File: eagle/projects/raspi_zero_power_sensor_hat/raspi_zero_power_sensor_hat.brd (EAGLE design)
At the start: 65 x 30 mm, 156 parts, among them J301 MOL-SL-2-RA, J302 USB_MICROB_RECPT, J401 MOL-SL-2-RA, J402 MOL-SL-2-V, J601 RECEPTACLE-2x5-2.54MM, J602 MOL-SL-4-RA, J603 MOL-SL-3-V, J604 RECEPTACLE-2x3-2.54MM, Q301 SSM6N7002KFU, Q401 SSM6N7002KFU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

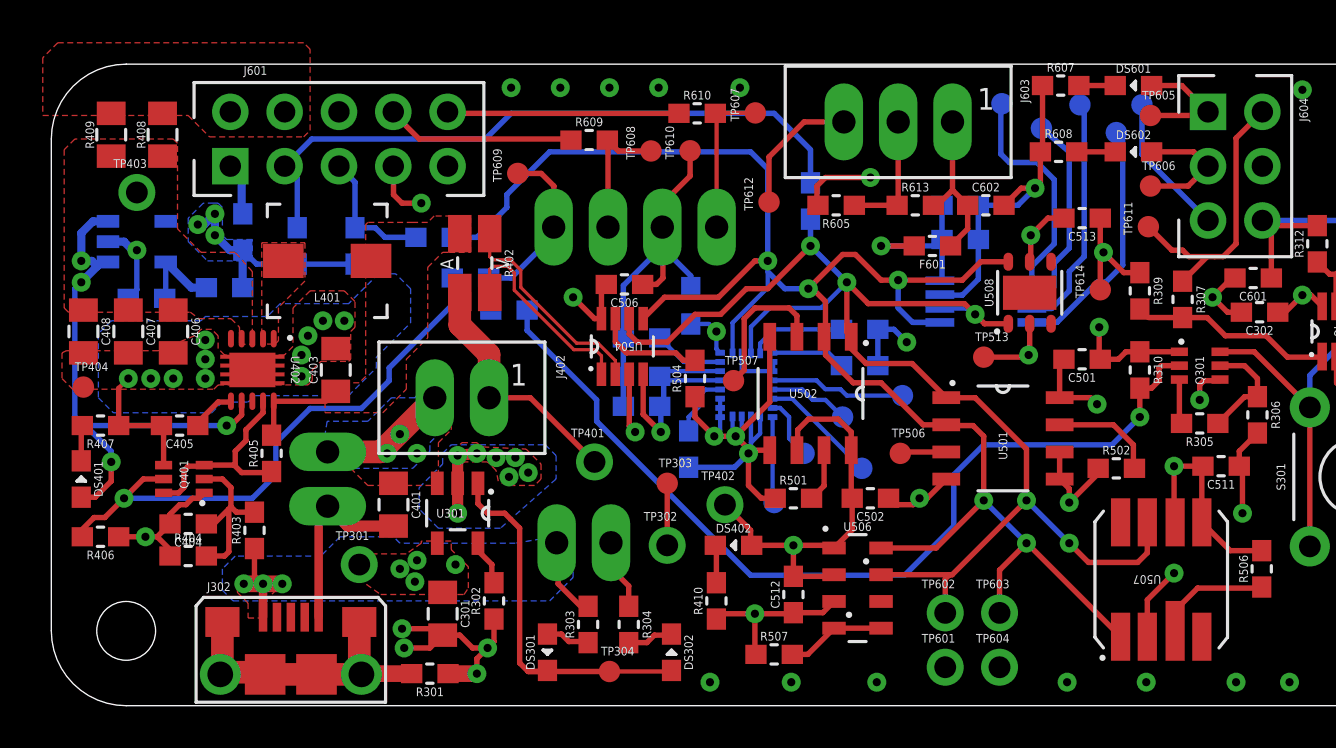
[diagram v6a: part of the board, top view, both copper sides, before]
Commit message: changed board outline to be added only on the board. modified the Raspi outline schematic symbol to only include the mouting holes
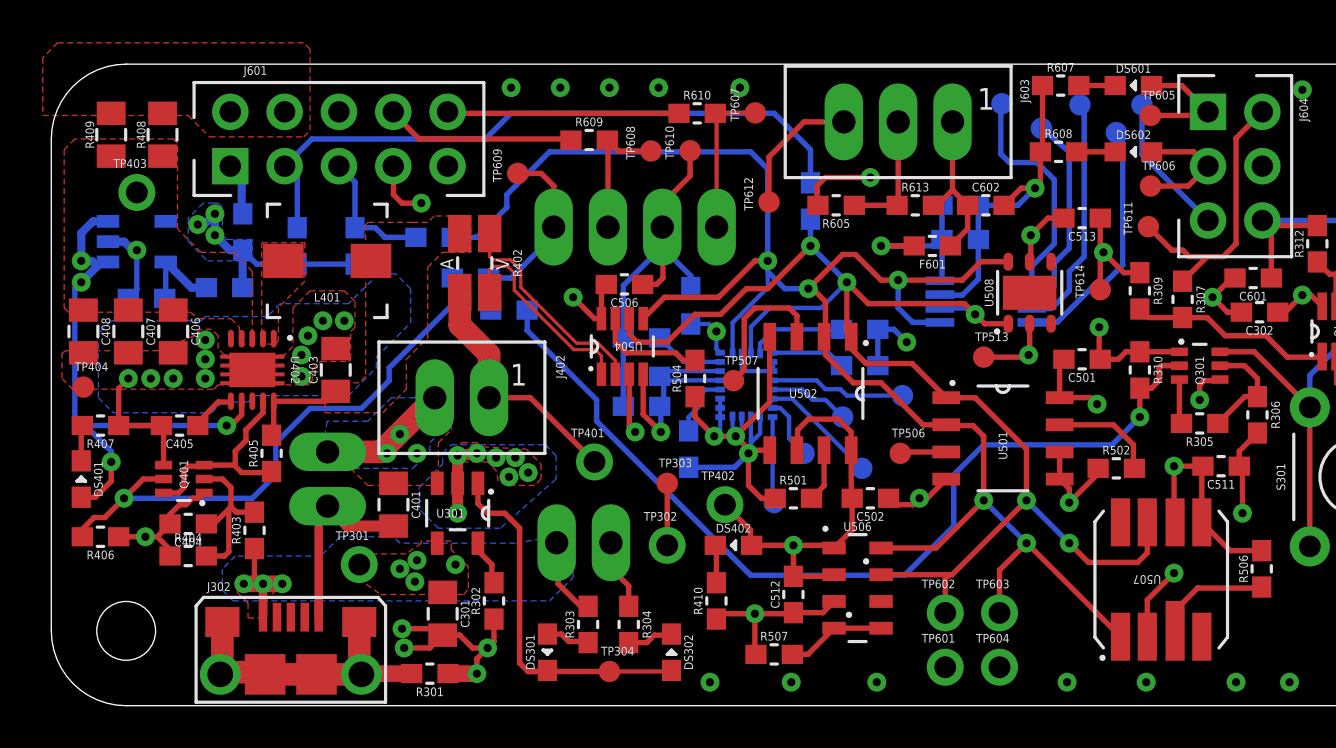
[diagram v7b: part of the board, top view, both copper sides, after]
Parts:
- removed OUTLINE601: RASPI-ZERO-3STANDOFFS-0CAM, daqcs:RASPI_ZERO_3STANDOFFS
- added OUTLINE1: RASPI_ZERO_OUTLINE_3S0C_ONLY, daqcs:RASPI_ZERO_3STANDOFFS_ONLY
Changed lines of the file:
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@@
 <grid distance="0.1" unitdist="mm" unit="mm" style="lines" multiple="1" display="no" altdistance="0.01" altunitdist="mm" altunit="mm"/>
 <layers>
-<layer number="1" name="Top" color="4" fill="1" visible="no" active="yes"/>
+<layer number="1" name="Top" color="4" fill="1" visible="yes" active="yes"/>
 <layer number="2" name="GND" color="26" fill="1" visible="no" active="yes"/>
 <layer number="3" name="Route3" color="4" fill="3" visible="no" active="no"/>
@@
 <layer number="19" name="Unrouted" color="6" fill="1" visible="no" active="yes"/>
 <layer number="20" name="Dimension" color="15" fill="1" visible="yes" active="yes"/>
-<layer number="21" name="tPlace" color="7" fill="1" visible="no" active="yes"/>
+<layer number="21" name="tPlace" color="7" fill="1" visible="yes" active="yes"/>
 <layer number="22" name="bPlace" color="23" fill="1" visible="no" active="yes"/>
-<layer number="23" name="tOrigins" color="15" fill="1" visible="no" active="yes"/>
+<layer number="23" name="tOrigins" color="15" fill="1" visible="yes" active="yes"/>
 <layer number="24" name="bOrigins" color="15" fill="1" visible="no" active="yes"/>
-<layer number="25" name="tNames" color="7" fill="1" visible="no" active="yes"/>
+<layer number="25" name="tNames" color="7" fill="1" visible="yes" active="yes"/>
 <layer number="26" name="bNames" color="7" fill="1" visible="no" active="yes"/>
-<layer number="27" name="tValues" color="7" fill="1" visible="no" active="yes"/>
+<layer number="27" name="tValues" color="7" fill="1" visible="yes" active="yes"/>
 <layer number="28" name="bValues" color="7" fill="1" visible="no" active="yes"/>
-<layer number="29" name="tStop" color="7" fill="3" visible="no" active="yes"/>
+<layer number="29" name="tStop" color="7" fill="3" visible="yes" active="yes"/>
 <layer number="30" name="bStop" color="7" fill="6" visible="no" active="yes"/>
-<layer number="31" name="tCream" color="7" fill="4" visible="no" active="yes"/>
+<layer number="31" name="tCream" color="7" fill="4" visible="yes" active="yes"/>
 <layer number="32" name="bCream" color="7" fill="5" visible="no" active="yes"/>
-<layer number="33" name="tFinish" color="6" fill="3" visible="no" active="yes"/>
+<layer number="33" name="tFinish" color="6" fill="3" visible="yes" active="yes"/>
 <layer number="34" name="bFinish" color="6" fill="6" visible="no" active="yes"/>
-<layer number="35" name="tGlue" color="7" fill="4" visible="no" active="yes"/>
+<layer number="35" name="tGlue" color="7" fill="4" visible="yes" active="yes"/>
 <layer number="36" name="bGlue" color="7" fill="5" visible="no" active="yes"/>
-<layer number="37" name="tTest" color="7" fill="1" visible="no" active="yes"/>
+<layer number="37" name="tTest" color="7" fill="1" visible="yes" active="yes"/>
 <layer number="38" name="bTest" color="7" fill="1" visible="no" active="yes"/>
-<layer number="39" name="tKeepout" color="4" fill="11" visible="no" active="yes"/>
+<layer number="39" name="tKeepout" color="4" fill="11" visible="yes" active="yes"/>
 <layer number="40" name="bKeepout" color="1" fill="11" visible="no" active="yes"/>
-<layer number="41" name="tRestrict" color="4" fill="10" visible="no" active="yes"/>
+<layer number="41" name="tRestrict" color="4" fill="10" visible="yes" active="yes"/>
 <layer number="42" name="bRestrict" color="1" fill="10" visible="no" active="yes"/>
 <layer number="43" name="vRestrict" color="2" fill="10" visible="no" active="yes"/>
-<layer number="44" name="Drills" color="7" fill="1" visible="no" active="yes"/>
+<layer number="44" name="Drills" color="7" fill="1" visible="yes" active="yes"/>
 <layer number="45" name="Holes" color="7" fill="1" visible="yes" active="yes"/>
-<layer number="46" name="Milling" color="3" fill="1" visible="no" active="yes"/>
-<layer number="47" name="Measures" color="7" fill="1" visible="no" active="yes"/>
-<layer number="48" name="Document" color="7" fill="1" visible="no" active="yes"/>
-<layer number="49" name="Reference" color="7" fill="1" visible="no" active="yes"/>
+<layer number="46" name="Milling" color="3" fill="1" visible="yes" active="yes"/>
+<layer number="47" name="Measures" color="7" fill="1" visible="yes" active="yes"/>
+<layer number="48" name="Document" color="7" fill="1" visible="yes" active="yes"/>
+<layer number="49" name="Reference" color="7" fill="1" visible="yes" active="yes"/>
 <layer number="50" name="dxf" color="7" fill="1" visible="no" active="no"/>
-<layer number="51" name="tDocu" color="14" fill="1" visible="no" active="yes"/>
+<layer number="51" name="tDocu" color="14" fill="1" visible="yes" active="yes"/>
 <layer number="52" name="bDocu" color="6" fill="1" visible="no" active="yes"/>
 <layer number="53" name="tGND_GNDA" color="7" fill="9" visible="no" active="no"/>
@@
 <board>
 <plain>
+<wire x1="3.5" y1="0" x2="0" y2="3.5" width="0" layer="20" curve="-90"/>
+<wire x1="65" y1="3.5" x2="61.5" y2="0" width="0" layer="20" curve="-90"/>
+<wire x1="61.5" y1="30" x2="65" y2="26.5" width="0" layer="20" curve="-90"/>
+<wire x1="0" y1="26.5" x2="3.5" y2="30" width="0" layer="20" curve="-90"/>
+<wire x1="3.5" y1="30" x2="61.5" y2="30" width="0" layer="20"/>
+<wire x1="65" y1="26.5" x2="65" y2="3.5" width="0" layer="20"/>
+<wire x1="61.5" y1="0" x2="3.5" y2="0" width="0" layer="20"/>
+<wire x1="0" y1="3.5" x2="0" y2="26.5" width="0" layer="20"/>
 </plain>
 <attributes>
@@
 <attribute name="DATASHEET" value="HW/docs/projects/raspi_zero_power_sensor_hat/datasheets/passives/c02e.pdf" x="48.2" y="22.8" size="1.778" layer="27" rot="R180" display="off"/>
 </element>
-<element name="OUTLINE601" library="daqcs" package="RASPI_ZERO_3STANDOFFS" value="RASPI-ZERO-3STANDOFFS-0CAM" x="0" y="0"/>
 <element name="DS601" library="daqcs" package="LED0603" value="YELLOW" x="50.6" y="29">
 <attribute name="FORWARD_CURRENT" value="20mA" x="50.6" y="29" size="1.778" layer="27" display="off"/>
@@
 <attribute name="TP_SIGNAL_NAME" value="" x="43.6" y="16.3" size="1.778" layer="27" display="off"/>
 </element>
+<element name="OUTLINE1" library="daqcs" package="RASPI_ZERO_3STANDOFFS_ONLY" value="RASPI_ZERO_OUTLINE_3S0C_ONLY" x="0" y="0"/>
 </elements>
 <signals>

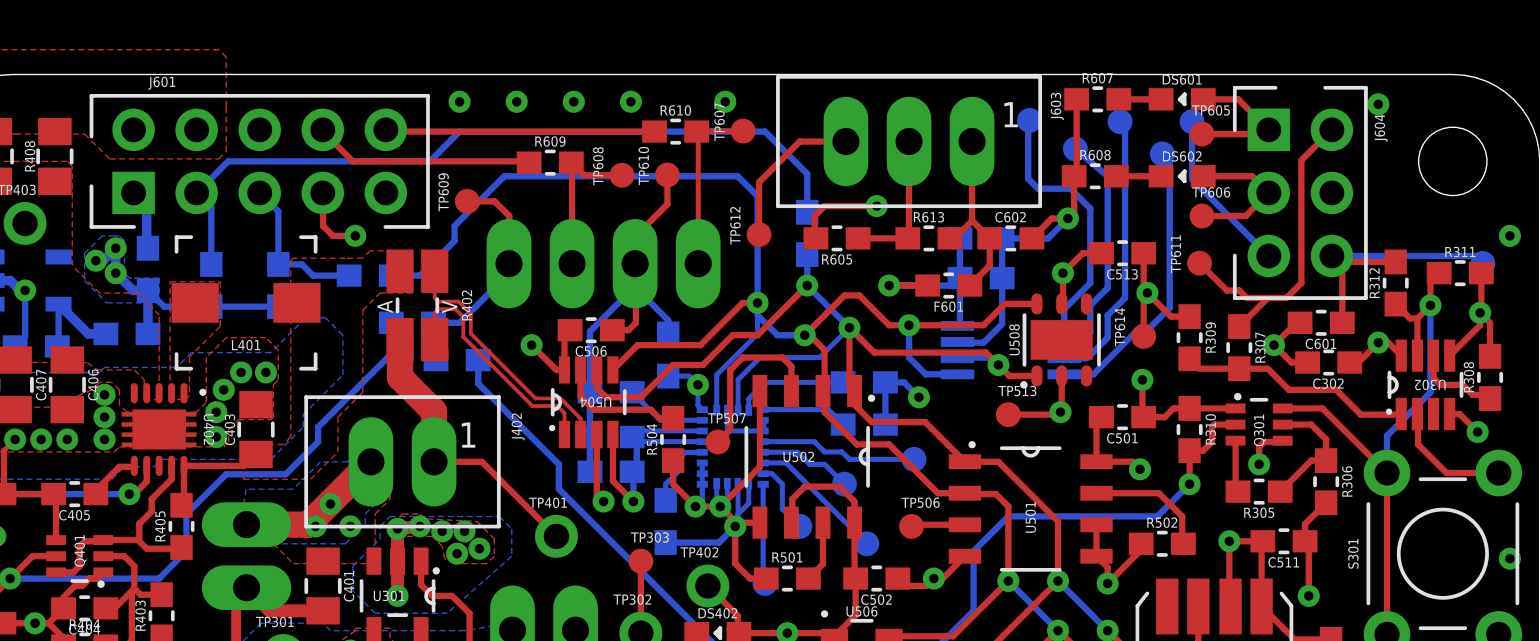
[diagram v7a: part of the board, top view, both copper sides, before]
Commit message: fixed bottom side component silk screen. SIZE * RATIO > 0.15mm
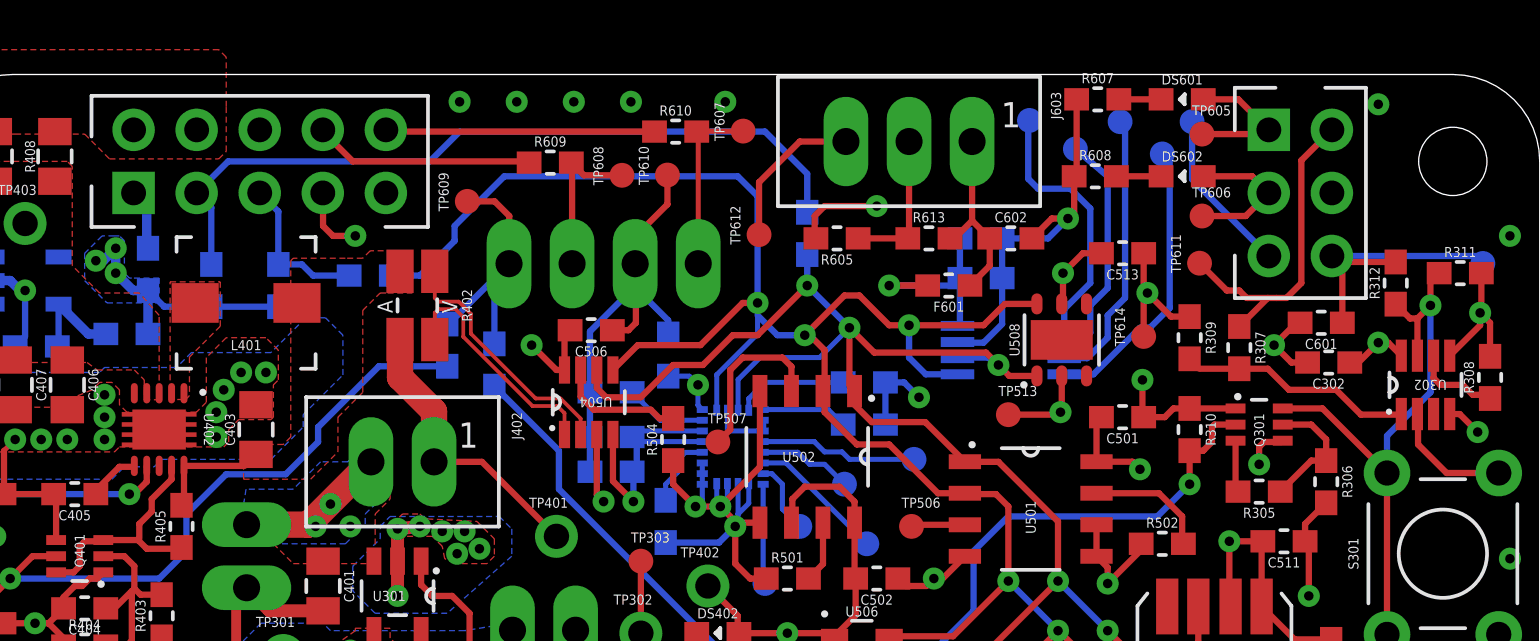
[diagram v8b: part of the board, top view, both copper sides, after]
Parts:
- moved R611 1.66 mm to (21.0, 19.1), turned to 270 degrees
- moved R612 1.51 mm to (22.9, 18.3), turned to 270 degrees
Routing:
- net MCU_TO_RASPI_RESET: track 43.4 -> 42.1 mm
- net MCU_TO_HAT_RESET: track 9.65 -> 10.8 mm
- net MCU_TO_BST_RESET: track 26.8 -> 27.5 mm
